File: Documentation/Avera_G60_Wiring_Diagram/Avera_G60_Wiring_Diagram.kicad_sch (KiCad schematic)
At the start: 9 parts

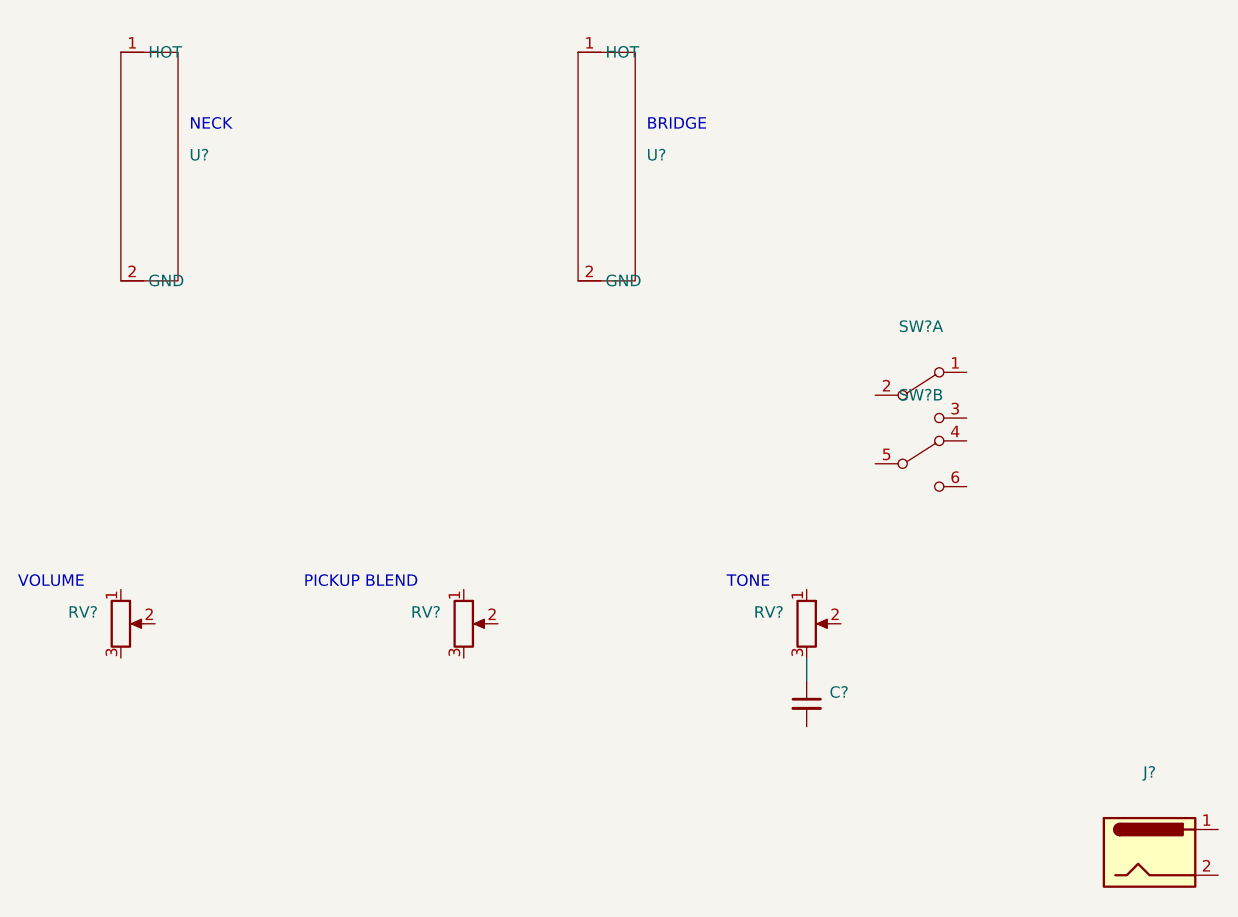
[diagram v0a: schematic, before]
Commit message: rough trace-out of wiring
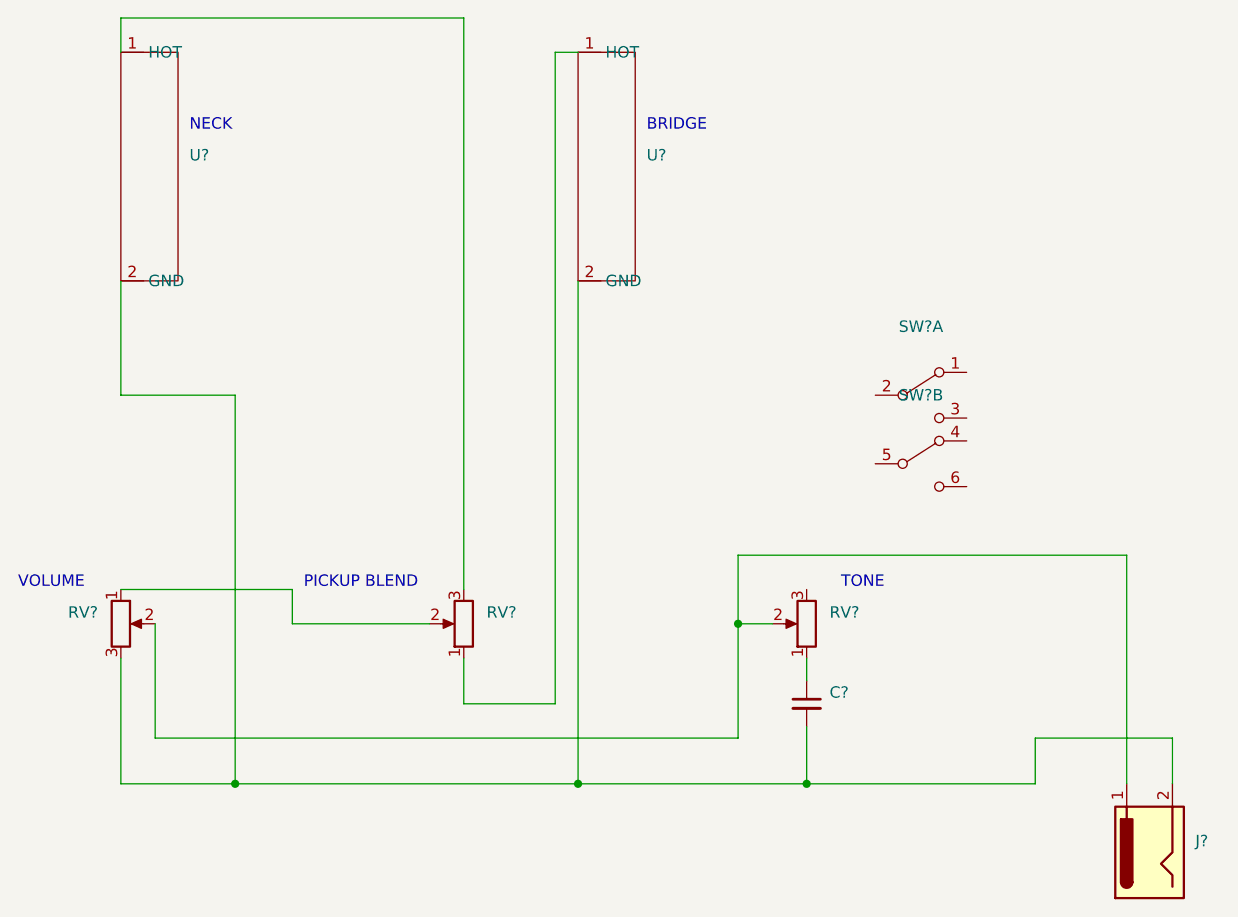
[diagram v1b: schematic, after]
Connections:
- net at J?.1: now also RV?.2, RV?.2
- net at J?.2: now also C?.2, RV?.3, U?.2 (GND), U?.2 (GND)
- net at U?.1 (HOT): now also RV?.1
- net at RV?.1: now also C?.1
- net at RV?.3: no longer C?.1
- net at U?.1 (HOT): now also RV?.3
- net at RV?.2: now also RV?.1
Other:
- moved on the sheet: J?, RV?
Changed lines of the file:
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@@
 (kicad_sch (version 20211123) (generator eeschema)
   (paper "A4")
+  (junction (at 165.1 132.08) (diameter 0) (color 0 0 0 0)
+  )
+  (junction (at 139.7 132.08) (diameter 0) (color 0 0 0 0)
+  )
+  (junction (at 157.48 114.3) (diameter 0) (color 0 0 0 0)
+  )
+  (junction (at 101.6 132.08) (diameter 0) (color 0 0 0 0)
+  )
+  (wire (pts (xy 205.74 127) (xy 205.74 132.08))
+    (stroke (width 0) (type default) (color 0 0 0 0))
+  )
+  (wire (pts (xy 92.71 114.3) (xy 92.71 127))
+    (stroke (width 0) (type default) (color 0 0 0 0))
+  )
+  (wire (pts (xy 137.16 50.8) (xy 137.16 123.19))
+    (stroke (width 0) (type default) (color 0 0 0 0))
+  )
+  (wire (pts (xy 200.66 106.68) (xy 200.66 132.08))
+    (stroke (width 0) (type default) (color 0 0 0 0))
+  )
+  (wire (pts (xy 157.48 106.68) (xy 200.66 106.68))
+    (stroke (width 0) (type default) (color 0 0 0 0))
+  )
+  (wire (pts (xy 157.48 127) (xy 157.48 114.3))
+    (stroke (width 0) (type default) (color 0 0 0 0))
+  )
+  (wire (pts (xy 101.6 88.9) (xy 88.9 88.9))
+    (stroke (width 0) (type default) (color 0 0 0 0))
+  )
+  (wire (pts (xy 88.9 50.8) (xy 88.9 46.99))
+    (stroke (width 0) (type default) (color 0 0 0 0))
+  )
+  (wire (pts (xy 190.5 132.08) (xy 190.5 127))
+    (stroke (width 0) (type default) (color 0 0 0 0))
+  )
+  (wire (pts (xy 127 118.11) (xy 127 123.19))
+    (stroke (width 0) (type default) (color 0 0 0 0))
+  )
+  (wire (pts (xy 92.71 127) (xy 157.48 127))
+    (stroke (width 0) (type default) (color 0 0 0 0))
+  )
+  (wire (pts (xy 139.7 50.8) (xy 137.16 50.8))
+    (stroke (width 0) (type default) (color 0 0 0 0))
+  )
   (wire (pts (xy 165.1 118.11) (xy 165.1 120.65))
     (stroke (width 0) (type default) (color 0 0 0 0))
   )
-  (text "TONE" (at 156.21 110.49 0)
+  (wire (pts (xy 190.5 127) (xy 205.74 127))
+    (stroke (width 0) (type default) (color 0 0 0 0))
+  )
+  (wire (pts (xy 88.9 76.2) (xy 88.9 88.9))
+    (stroke (width 0) (type default) (color 0 0 0 0))
+  )
+  (wire (pts (xy 165.1 125.73) (xy 165.1 132.08))
+    (stroke (width 0) (type default) (color 0 0 0 0))
+  )
+  (wire (pts (xy 107.95 114.3) (xy 107.95 110.49))
+    (stroke (width 0) (type default) (color 0 0 0 0))
+  )
+  (wire (pts (xy 88.9 110.49) (xy 107.95 110.49))
+    (stroke (width 0) (type default) (color 0 0 0 0))
+  )
+  (wire (pts (xy 139.7 76.2) (xy 139.7 132.08))
+    (stroke (width 0) (type default) (color 0 0 0 0))
+  )
+  (wire (pts (xy 139.7 132.08) (xy 101.6 132.08))
+    (stroke (width 0) (type default) (color 0 0 0 0))
+  )
+  (wire (pts (xy 123.19 114.3) (xy 107.95 114.3))
+    (stroke (width 0) (type default) (color 0 0 0 0))
+  )
+  (wire (pts (xy 127 46.99) (xy 127 110.49))
+    (stroke (width 0) (type default) (color 0 0 0 0))
+  )
+  (wire (pts (xy 165.1 132.08) (xy 190.5 132.08))
+    (stroke (width 0) (type default) (color 0 0 0 0))
+  )
+  (wire (pts (xy 88.9 46.99) (xy 127 46.99))
+    (stroke (width 0) (type default) (color 0 0 0 0))
+  )
+  (wire (pts (xy 157.48 114.3) (xy 157.48 106.68))
+    (stroke (width 0) (type default) (color 0 0 0 0))
+  )
+  (wire (pts (xy 139.7 132.08) (xy 165.1 132.08))
+    (stroke (width 0) (type default) (color 0 0 0 0))
+  )
+  (wire (pts (xy 157.48 114.3) (xy 161.29 114.3))
+    (stroke (width 0) (type default) (color 0 0 0 0))
+  )
+  (wire (pts (xy 101.6 132.08) (xy 101.6 88.9))
+    (stroke (width 0) (type default) (color 0 0 0 0))
+  )
+  (wire (pts (xy 88.9 132.08) (xy 101.6 132.08))
+    (stroke (width 0) (type default) (color 0 0 0 0))
+  )
+  (wire (pts (xy 88.9 118.11) (xy 88.9 132.08))
+    (stroke (width 0) (type default) (color 0 0 0 0))
+  )
+  (wire (pts (xy 137.16 123.19) (xy 127 123.19))
+    (stroke (width 0) (type default) (color 0 0 0 0))
+  )
+  (text "TONE" (at 168.91 110.49 0)
     (effects (font (size 1.27 1.27)) (justify left bottom))
   )
@@
     (pin "6")
   )
-  (symbol (lib_id "Connector:Jack-DC") (at 203.2 139.7 0) (unit 1)
-    (in_bom yes) (on_board yes) (fields_autoplaced)
-    (property "Reference" "J?" (id 0) (at 203.2 130.81 0))
-    (property "Value" "" (id 1) (at 203.2 133.35 0))
-    (property "Footprint" "" (id 2) (at 204.47 140.716 0)
-      (effects (font (size 1.27 1.27)) hide)
-    )
-    (property "Datasheet" "~" (id 3) (at 204.47 140.716 0)
+  (symbol (lib_id "Connector:Jack-DC") (at 203.2 139.7 90) (unit 1)
+    (in_bom yes) (on_board yes) (fields_autoplaced)
+    (property "Reference" "J?" (id 0) (at 208.28 138.4299 90)
+      (effects (font (size 1.27 1.27)) (justify right))
+    )
+    (property "Value" "" (id 1) (at 208.28 140.9699 90)
+      (effects (font (size 1.27 1.27)) (justify right))
+    )
+    (property "Footprint" "" (id 2) (at 204.216 138.43 0)
+      (effects (font (size 1.27 1.27)) hide)
+    )
+    (property "Datasheet" "~" (id 3) (at 204.216 138.43 0)
       (effects (font (size 1.27 1.27)) hide)
     )
@@
     (pin "2")
   )
-  (symbol (lib_id "Device:R_Potentiometer") (at 165.1 114.3 0) (unit 1)
-    (in_bom yes) (on_board yes) (fields_autoplaced)
-    (property "Reference" "RV?" (id 0) (at 162.56 113.0299 0)
-      (effects (font (size 1.27 1.27)) (justify right))
-    )
-    (property "Value" "" (id 1) (at 162.56 115.5699 0)
+  (symbol (lib_id "Device:R_Potentiometer") (at 165.1 114.3 180) (unit 1)
+    (in_bom yes) (on_board yes) (fields_autoplaced)
+    (property "Reference" "RV?" (id 0) (at 167.64 113.0299 0)
+      (effects (font (size 1.27 1.27)) (justify right))
+    )
+    (property "Value" "" (id 1) (at 167.64 115.5699 0)
       (effects (font (size 1.27 1.27)) (justify right))
     )
@@
     (pin "2")
   )
-  (symbol (lib_id "Device:R_Potentiometer") (at 127 114.3 0) (unit 1)
-    (in_bom yes) (on_board yes) (fields_autoplaced)
-    (property "Reference" "RV?" (id 0) (at 124.46 113.0299 0)
-      (effects (font (size 1.27 1.27)) (justify right))
-    )
-    (property "Value" "" (id 1) (at 124.46 115.5699 0)
-      (effects (font (size 1.27 1.27)) (justify right))
-    )
+  (symbol (lib_id "Device:R_Potentiometer") (at 127 114.3 180) (unit 1)
+    (in_bom yes) (on_board yes) (fields_autoplaced)
+    (property "Reference" "RV?" (id 0) (at 129.54 113.0299 0)
+      (effects (font (size 1.27 1.27)) (justify right))
+    )
+    (property "Value" "" (id 1) (at 129.54 115.5699 0)
+      (effects (font (size 1.27 1.27)) (justify right))
+    )
